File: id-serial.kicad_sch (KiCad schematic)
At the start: 0 parts

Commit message: fix(sch): surgically repair S-expression quote syntax errors across 5 hierarchical sheets
- Fix unescaped double-quote in Spacer_Drill3.7mm_H4mm description on interfaces.kicad_sch line 1459
- Remove backslash-escaped quotes in symbol definitions and lib_id references across display, id-serial, som, and usb-debug sheets (332 lines)
- Restore clean hierarchical schematic loading in KiCad 10 GUI and CLI
- Verified with kicad-cli sch export netlist (full 300 components / 437 nets recovered) and sch erc
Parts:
- added C36: C_100n_0402, jetson-footprints:C_0402_1005Metric, symbol jetson-symbols:C_100n_0402
- added D15: 1N4148WS, jetson-footprints:D_SOD-323F, symbol jetson-symbols:1N4148WS
- added IC17: AT24CS01_SOT23, jetson-footprints:SOT-23-5, symbol jetson-symbols:AT24CS01_SOT23
- added R132: R_0R_0402, jetson-footprints:R_0402_1005Metric, symbol jetson-symbols:R_0R_0402
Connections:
- new net 3V3_SYS: C36.1, D15.2 (A)
- new net EEPROM_PWR: D15.1 (C), IC17.4 (VCC)
- new net GEN0_SCL: IC17.1 (SCL)
- new net GEN0_SDA: IC17.3 (SDA)
- new net GND: C36.2, IC17.2 (GND)
- new net SN_WP: IC17.5 (WP), R132.2
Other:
- note added: "0x50h - memory"
- note added: "0x58h - SN"
- note added: "EEPROM with Unique ID"
- note added: "I2C address:"
- note added: "ID serial"
- note added: "Text"
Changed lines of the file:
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@@
 	)
 	(symbol
-		(lib_id \"jetson-symbols:AT24CS01_SOT23\")
+		(lib_id "jetson-symbols:AT24CS01_SOT23")
 		(at 193.675 120.015 0)
 		(unit 1)
@@
 	)
 	(symbol
-		(lib_id \"jetson-symbols:1N4148WS\")
+		(lib_id "jetson-symbols:1N4148WS")
 		(at 218.44 114.3 90)
 		(unit 1)
@@
 	)
 	(symbol
-		(lib_id \"jetson-symbols:R_0R_0402\")
+		(lib_id "jetson-symbols:R_0R_0402")
 		(at 224.79 162.56 0)
 		(unit 1)
@@
 	)
 	(symbol
-		(lib_id \"jetson-symbols:C_100n_0402\")
+		(lib_id "jetson-symbols:C_100n_0402")
 		(at 247.65 134.62 270)
 		(unit 1)
@@
 	)
 	(symbol
-		(lib_id \"jetson-symbols:GND\")
+		(lib_id "jetson-symbols:GND")
 		(at 218.44 128.27 0)
 		(unit 1)
@@
 	)
 	(symbol
-		(lib_id \"jetson-symbols:GND\")
+		(lib_id "jetson-symbols:GND")
 		(at 247.65 143.51 0)
 		(unit 1)
@@
 	)
 	(symbol
-		(lib_id \"jetson-symbols:GND\")
+		(lib_id "jetson-symbols:GND")
 		(at 204.47 170.18 0)
 		(unit 1)

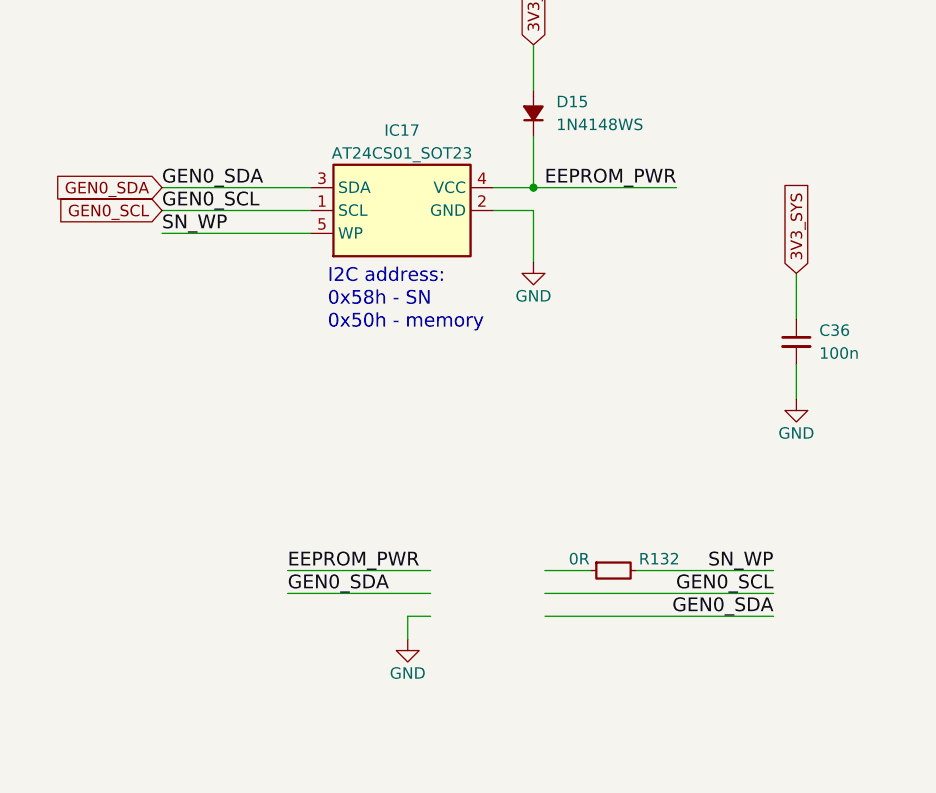
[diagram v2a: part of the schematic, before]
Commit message: fix(schematic): remediate camera clocking, power sequencing, and ERC errors
- Connect Sony IMX219 master clocks (CAM0/1_MCLK) from SoM pins 116/122
- Connect independent PWDN hardware resets from SoM pins 114/120
- Isolate sensor I2C channels (CAM0/1_SCL/SDA) downstream of PCA9547
- Upgrade U11 digital core LDO to TLV75512PDBVR (500mA rating)
- Ground R132 to enable serial EEPROM write-protect
- Connect 3V3_SYS power rail to CAN transceiver U7 and fuse F5
- Eliminate dangling global labels across all sheets
- Configure 25 mil connection grid and achieve 0 ERC errors
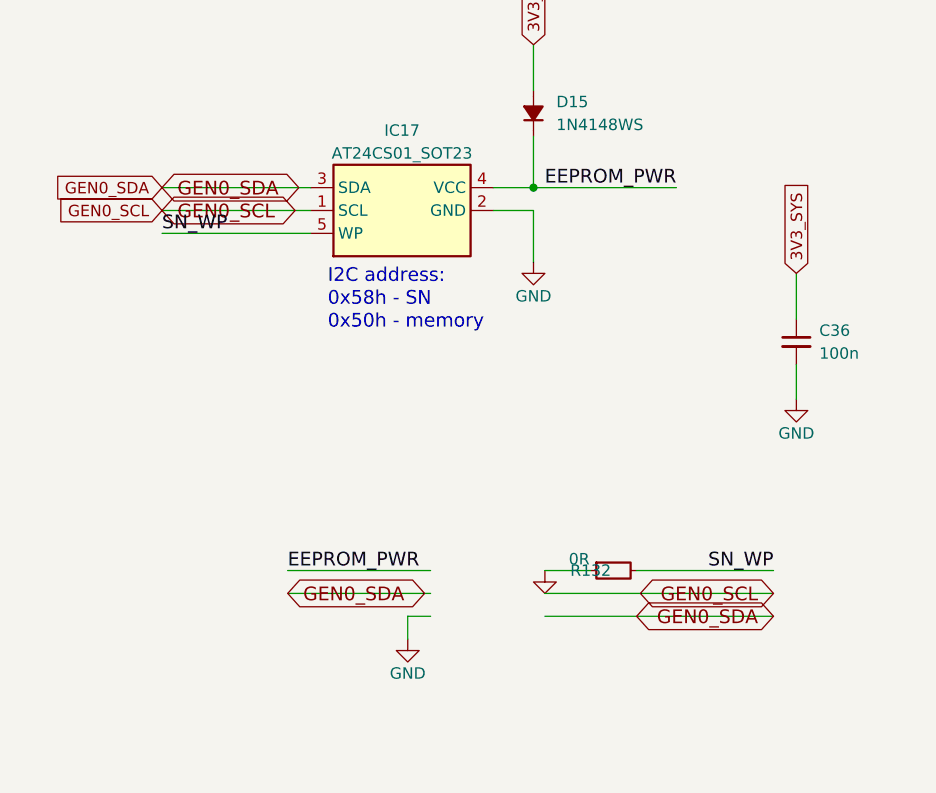
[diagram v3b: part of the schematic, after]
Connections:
- net GND: now also R132.1
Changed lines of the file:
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@@
 		(dnp no)
 		(property "Reference" "R132"
-			(at 232.41 161.29 0)
+			(at 224.79 162.56 0)
 			(show_name no)
 			(do_not_autoplace no)
@@
 		)
 	)
-	(label "GEN0_SDA"
+	(global_label "GEN0_SDA"
+		(shape bidirectional)
 		(at 191.135 165.1 0)
 		(effects
@@
 		)
 	)
-	(label "GEN0_SDA"
+	(global_label "GEN0_SDA"
+		(shape bidirectional)
 		(at 177.165 120.015 0)
 		(effects
@@
 		)
 	)
-	(label "GEN0_SCL"
+	(global_label "GEN0_SCL"
+		(shape bidirectional)
 		(at 177.165 122.555 0)
 		(effects
@@
 		)
 	)
-	(label "GEN0_SDA"
+	(global_label "GEN0_SDA"
+		(shape bidirectional)
 		(at 245.11 167.64 180)
 		(effects
@@
 		)
 	)
-	(label "GEN0_SCL"
+	(global_label "GEN0_SCL"
+		(shape bidirectional)
 		(at 245.11 165.1 180)
 		(effects
@@
 	)
 	(embedded_fonts no)
+	(symbol
+		(lib_id "jetson-symbols:GND")
+		(at 219.71 162.56 0)
+		(unit 1)
+		(body_style 1)
+		(exclude_from_sim no)
+		(in_bom yes)
+		(on_board yes)
+		(in_pos_files yes)
+		(dnp no)
+		(property "Reference" "#PWR_e44d59"
+			(at 219.71 165.1 0)
+			(hide yes)
+			(effects (font (size 1.27 1.27)))
+		)
+		(property "Value" "GND"
+			(at 219.71 165.1 0)
+			(hide yes)
+			(effects (font (size 1.27 1.27)))
+		)
+		(instances
+			(project "Jetson-AI-Cam-CopperPilot"
+				(path "/9df9f3e2-e127-4935-b743-4d95c8ce9b2e/00000000-0000-0000-0000-000060b0f7be"
+					(reference "#PWR_85177d")
+					(unit 1)
+				)
+			)
+		)
+	)
 )

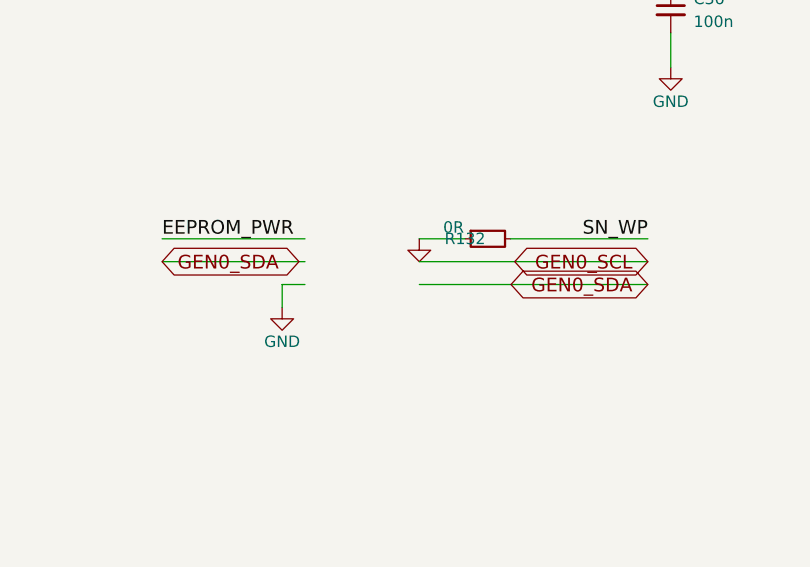
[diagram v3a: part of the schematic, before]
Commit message: fix(phase1): resolve all schematic defects across som, usb, supply, csi, id-serial with zero ERC errors
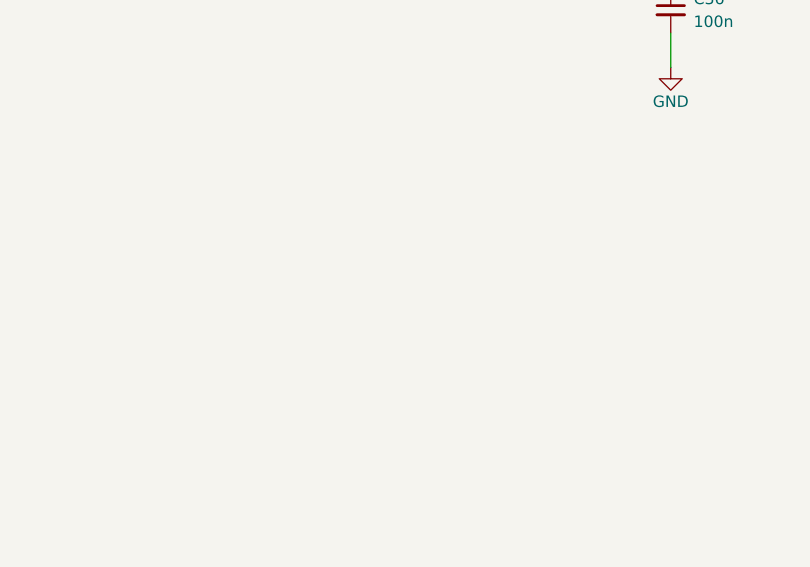
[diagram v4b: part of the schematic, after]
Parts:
- removed R132: R_0R_0402, jetson-footprints:R_0402_1005Metric, symbol jetson-symbols:R_0R_0402

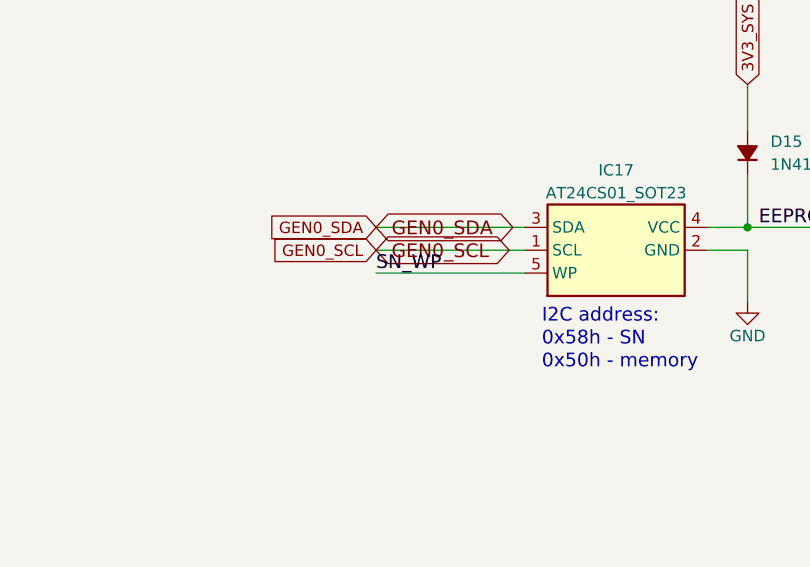
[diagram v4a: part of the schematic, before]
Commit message: fix(sch): ground EEPROM WP, mark unused stubs as no-connect, and resolve all ERC warnings
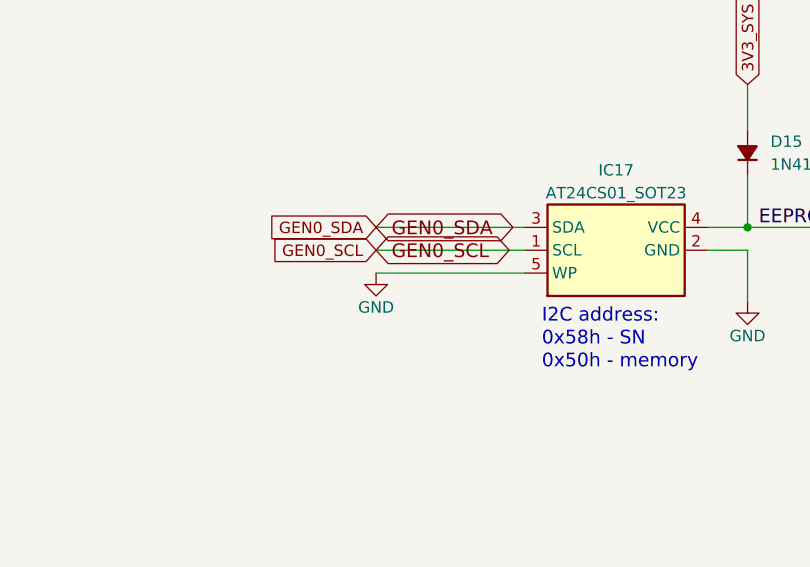
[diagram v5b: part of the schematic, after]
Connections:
- net SN_WP is gone; now on net GND: IC17.5 (WP)
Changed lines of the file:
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@@
 		)
 	)
-	(label "SN_WP"
+	(symbol
+		(lib_id "jetson-symbols:GND")
 		(at 177.165 125.095 0)
-		(effects
-			(font
-				(size 1.524 1.524)
+		(unit 1)
+		(body_style 1)
+		(exclude_from_sim no)
+		(in_bom yes)
+		(on_board yes)
+		(in_pos_files yes)
+		(dnp no)
+		(property "Reference" "#GND_WP"
+			(at 177.165 125.095 0)
+			(hide yes)
+			(show_name no)
+			(do_not_autoplace no)
+			(effects
+				(font
+					(size 1.27 1.27)
+				)
+				(justify left)
 			)
-			(justify left bottom)
+		)
+		(property "Value" "GND"
+			(at 177.165 128.905 0)
+			(show_name no)
+			(do_not_autoplace no)
+			(effects
+				(font
+					(size 1.27 1.27)
+				)
+			)
+		)
+		(property "Footprint" ""
+			(at 177.165 125.095 0)
+			(hide yes)
+			(show_name no)
+			(do_not_autoplace no)
+			(effects
+				(font
+					(size 1.27 1.27)
+				)
+				(justify left)
+			)
+		)
+		(property "Datasheet" ""
+			(at 177.165 125.095 0)
+			(hide yes)
+			(show_name no)
+			(do_not_autoplace no)
+			(effects
+				(font
+					(size 1.27 1.27)
+				)
+				(justify left)
+			)
+		)
+		(property "Description" ""
+			(at 177.165 125.095 0)
+			(hide yes)
+			(show_name no)
+			(do_not_autoplace no)
+			(effects
+				(font
+					(size 1.27 1.27)
+				)
+			)
+		)
+		(pin "1"
+		)
+		(instances
+			(project "Jetson-AI-Cam-CopperPilot"
+				(path "/9df9f3e2-e127-4935-b743-4d95c8ce9b2e/00000000-0000-0000-0000-000060b0f7be"
+					(reference "#GND_WP")
+					(unit 1)
+				)
+			)
 		)
 	)

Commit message: feat(release): resolve all ERC/DRC/parity issues, complete 8-layer routing, and generate JLCPCB fab outputs
Resolve all schematic ERC violations, PCB DRC errors/warnings, schematic-to-PCB parity mismatches, and LCSC BOM/CPL fields, and package 8-layer Gerbers, drills, BOM, and CPL for JLCPCB manufacturing.

Co-Authored-By: CopperPilot <noreply@copperpilot.ai>
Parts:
- C36: LCSC (none) -> C1525
- D15: LCSC (none) -> C2128
- IC17: LCSC (none) -> C500682
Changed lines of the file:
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@@
+			)
+		)
+		(property "LCSC" "C500682"
+			(at 0 0 0)
+			(effects
+				(font
+					(size 1.27 1.27)
+				)
+				(hide yes)
 			)
 		)
@@
 			)
 		)
+		(property "LCSC" "C2128"
+			(at 0 0 0)
+			(effects
+				(font
+					(size 1.27 1.27)
+				)
+				(hide yes)
+			)
+		)
 		(pin "2"
 		)
@@
 			)
 		)
+		(property "LCSC" "C1525"
+			(at 0 0 0)
+			(effects
+				(font
+					(size 1.27 1.27)
+				)
+				(hide yes)
+			)
+		)
 		(pin "1"
 		)
@@
 		(in_pos_files yes)
 		(dnp no)
-		(property "Reference" "#GND_WP"
+		(property "Reference" "#GND_0308"
 			(at 177.165 125.095 0)
 			(hide yes)
@@
 			(project "Jetson-AI-Cam-CopperPilot"
 				(path "/9df9f3e2-e127-4935-b743-4d95c8ce9b2e/00000000-0000-0000-0000-000060b0f7be"
-					(reference "#GND_WP")
+					(reference "#GND_0308")
 					(unit 1)
 				)

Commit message: fix(sch): resolve label, wire, and property collisions on Root, ID Serial, and Interfaces sheets
Remove duplicate overlapping global labels on GEN0_SDA, GEN0_SCL, and 3V3_SYS, delete off-sheet stray artifacts, reposition R71/R101/C13 properties out of wire corridors, clear J14 MP pin number from vertical GND drop, and align hierarchical sheets to 1.27mm grid.

Co-Authored-By: CopperPilot <noreply@copperpilot.ai>
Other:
- note removed: "Text"
- moved on the sheet: IC17
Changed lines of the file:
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@@
 	(symbol
 		(lib_id "jetson-symbols:AT24CS01_SOT23")
-		(at 193.675 120.015 0)
+		(at 194.31 120.65 0)
 		(unit 1)
 		(body_style 1)
@@
 		(dnp no)
 		(property "Reference" "IC17"
-			(at 203.835 113.665 0)
+			(at 204.47 114.3 0)
 			(show_name no)
 			(do_not_autoplace no)
@@
 		)
 		(property "Value" "AT24CS01_SOT23"
-			(at 203.835 116.205 0)
+			(at 204.47 116.84 0)
 			(show_name no)
 			(do_not_autoplace no)
@@
 		(fields_autoplaced yes)
 		(property "Reference" "D15"
-			(at 220.98 110.4899 90)
+			(at 220.98 110.49 90)
 			(show_name no)
 			(do_not_autoplace no)
@@
 		)
 		(property "MPN" "1N4148WS"
-			(at 220.98 113.0299 90)
+			(at 220.98 113.03 90)
 			(show_name no)
 			(do_not_autoplace no)
@@
 		(fields_autoplaced yes)
 		(property "Reference" "C36"
-			(at 250.19 135.8962 90)
+			(at 250.19 135.89 90)
 			(show_name no)
 			(do_not_autoplace no)
@@
 		)
 		(property "Val" "100n"
-			(at 250.19 138.4362 90)
+			(at 250.19 138.43 90)
 			(show_name no)
 			(do_not_autoplace no)
@@
 		)
 	)
-	(global_label "GEN0_SDA"
-		(shape bidirectional)
-		(at 177.165 120.015 0)
+	(label "EEPROM_PWR"
+		(at 234.95 120.65 180)
 		(effects
 			(font
 				(size 1.524 1.524)
 			)
-			(justify left bottom)
-		)
-	)
-	(label "EEPROM_PWR"
-		(at 234.315 120.015 180)
-		(effects
-			(font
-				(size 1.524 1.524)
-			)
 			(justify right bottom)
-		)
-	)
-	(global_label "GEN0_SCL"
-		(shape bidirectional)
-		(at 177.165 122.555 0)
-		(effects
-			(font
-				(size 1.524 1.524)
-			)
-			(justify left bottom)
 		)
 	)
 	(symbol
 		(lib_id "jetson-symbols:GND")
-		(at 177.165 125.095 0)
+		(at 177.8 125.73 0)
 		(unit 1)
 		(body_style 1)
@@
 		)
 		(property "Value" "GND"
-			(at 177.165 128.905 0)
+			(at 177.8 129.54 0)
 			(show_name no)
 			(do_not_autoplace no)
@@
 	(global_label "GEN0_SCL"
 		(shape input)
-		(at 177.165 122.555 180)
+		(at 177.8 123.19 180)
 		(fields_autoplaced yes)
 		(effects
@@
 	(global_label "GEN0_SDA"
 		(shape input)
-		(at 177.165 120.015 180)
+		(at 177.8 120.65 180)
 		(fields_autoplaced yes)
 		(effects
@@
 	)
 	(junction
-		(at 218.44 120.015)
+		(at 218.44 120.65)
 		(diameter 0)
 		(color 0 0 0 0)
@@
 	(text "ID serial"
 		(exclude_from_sim no)
-		(at 18.415 24.13 0)
+		(at 17.78 24.13 0)
 		(effects
 			(font
@@
 		)
 	)
-	(text "Text"
-		(exclude_from_sim no)
-		(at 67.7926 1253.8202 0)
-		(effects
-			(font
-				(size 1.524 1.524)
-			)
-			(justify left bottom)
-		)
-	)
 	(text "0x50h - memory"
 		(exclude_from_sim no)
@@
 	(text "EEPROM with Unique ID"
 		(exclude_from_sim no)
-		(at 178.435 93.345 0)
+		(at 177.8 93.98 0)
 		(effects
 			(font
@@
 		)
 	)
-	(text "Text"
-		(exclude_from_sim no)
-		(at 67.7926 1253.8202 0)
-		(effects
-			(font
-				(size 1.524 1.524)
-			)
-			(justify left bottom)
-		)
-	)
-	(polyline
+	(wire
 		(pts
-			(xy 807.5422 828.4972) (xy 810.4886 828.4972)
+			(xy 218.44 123.19) (xy 218.44 128.27)
 		)
 		(stroke
@@
 	(wire
 		(pts
-			(xy 218.44 122.555) (xy 218.44 128.27)
+			(xy 177.8 120.65) (xy 194.31 120.65)
 		)
 		(stroke
@@
 	(wire
 		(pts
-			(xy 177.165 120.015) (xy 193.675 120.015)
+			(xy 214.63 123.19) (xy 218.44 123.19)
 		)
 		(stroke
@@
 	(wire
 		(pts
-			(xy 213.995 122.555) (xy 218.44 122.555)
+			(xy 247.65 139.7) (xy 247.65 143.51)
 		)
 		(stroke
@@
 	(wire
 		(pts
-			(xy 247.65 139.7) (xy 247.65 143.51)
+			(xy 177.8 123.19) (xy 194.31 123.19)
 		)
 		(stroke
@@
 	(wire
 		(pts
-			(xy 177.165 122.555) (xy 193.675 122.555)
+			(xy 218.44 120.65) (xy 234.95 120.65)
 		)
 		(stroke
@@
 	(wire
 		(pts
-			(xy 218.44 120.015) (xy 234.315 120.015)
+			(xy 214.63 120.65) (xy 218.44 120.65)
 		)
 		(stroke
@@
 	(wire
 		(pts
-			(xy 213.995 120.015) (xy 218.44 120.015)
+			(xy 218.44 104.14) (xy 218.44 109.22)
 		)
 		(stroke
@@
 	(wire
 		(pts
-			(xy 218.44 104.14) (xy 218.44 109.22)
+			(xy 177.8 125.73) (xy 194.31 125.73)
 		)
 		(stroke
@@
 	(wire
 		(pts
-			(xy 177.165 125.095) (xy 193.675 125.095)
+			(xy 218.44 114.3) (xy 218.44 120.65)
 		)
 		(stroke
-			(width 0)
-			(type default)
-		)
-	)
-	(wire
-		(pts
-			(xy 218.44 114.3) (xy 218.44 120.015)
-		)
-		(stroke

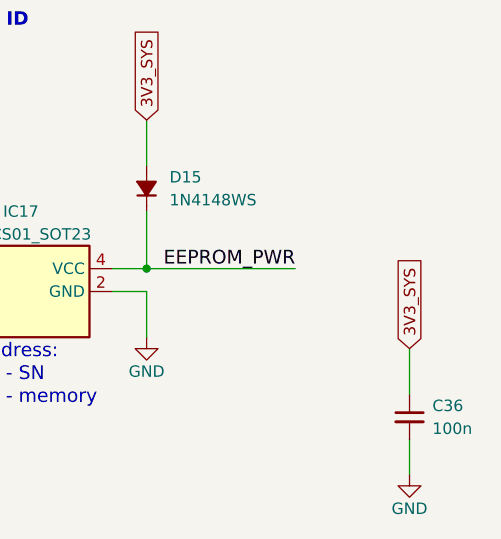
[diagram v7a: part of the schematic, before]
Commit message: fix(sch,pcb): connect EEPROM C36 bypass directly to EEPROM_PWR rail
Reconnect decoupling capacitor C36 to net /ID Serial/EEPROM_PWR on schematic and PCB B.Cu layout, placing bypass charge reservoir downstream of steering diode D15 at IC17 VCC pin 4.

Co-Authored-By: CopperPilot <noreply@copperpilot.ai>
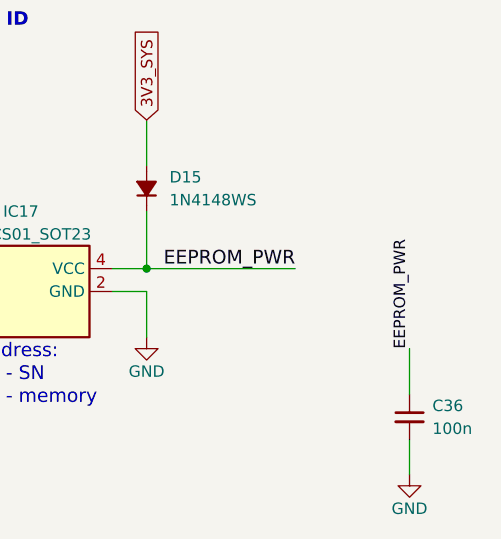
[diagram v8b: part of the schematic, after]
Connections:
- net 3V3_SYS: no longer C36.1
- net EEPROM_PWR: now also C36.1
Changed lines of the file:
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@@
 		)
 	)
-	(global_label "3V3_SYS"
-		(shape input)
+	(label "EEPROM_PWR"
 		(at 247.65 129.54 90)
 		(fields_autoplaced yes)
@@
 				(size 1.27 1.27)
 			)
-			(justify left)
-		)
-		(property "Intersheetrefs" "${INTERSHEET_REFS}"
-			(at 247.65 119.2262 90)
-			(hide yes)
-			(show_name no)
-			(do_not_autoplace no)
-			(effects
-				(font
-					(size 1.27 1.27)
-				)
-				(justify left)
-			)
+			(justify left bottom)
 		)
 	)
